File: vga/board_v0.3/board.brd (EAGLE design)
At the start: 55 x 53 mm, 130 parts, among them IC1 XC6S{9,16,25}LX-FT256, IC2 74LVC3G34, IC3 AS4C8M16D1

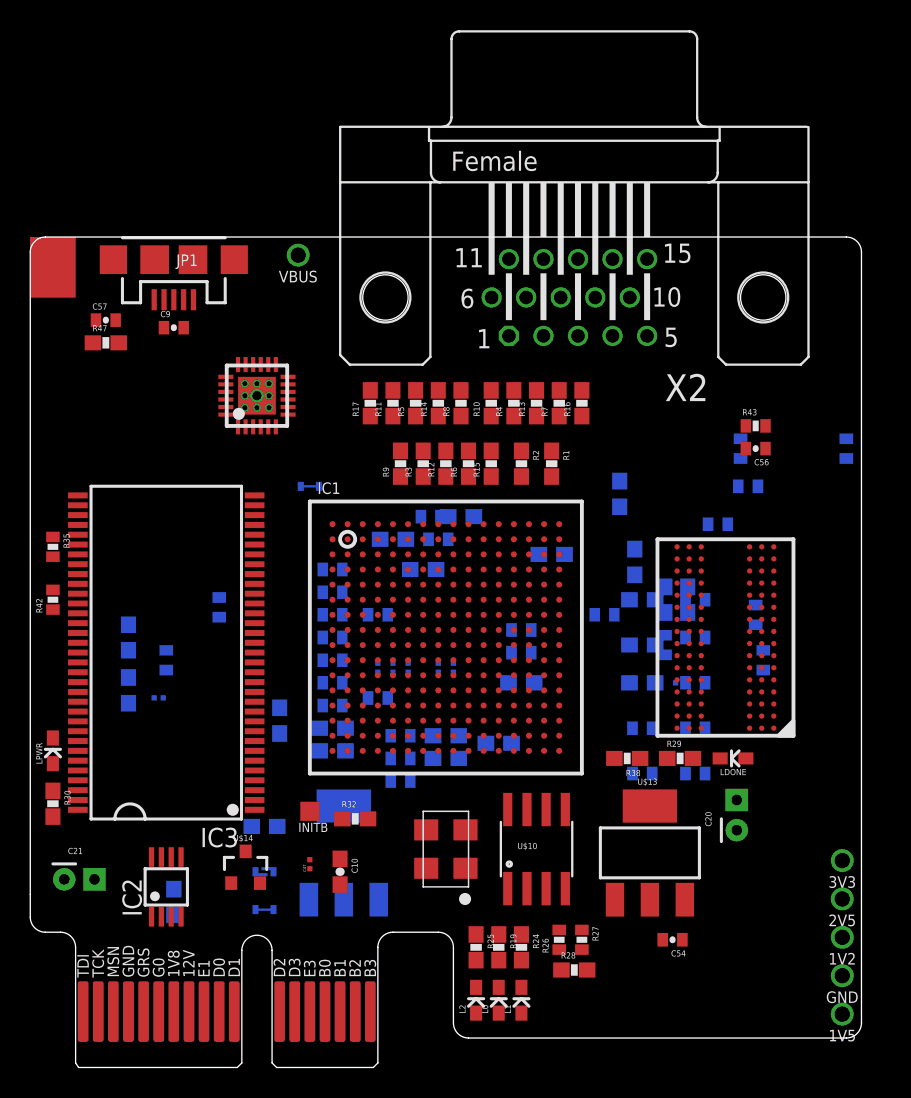
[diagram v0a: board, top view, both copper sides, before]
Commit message: vga board v0.3.  added keepout to a bunch of packages
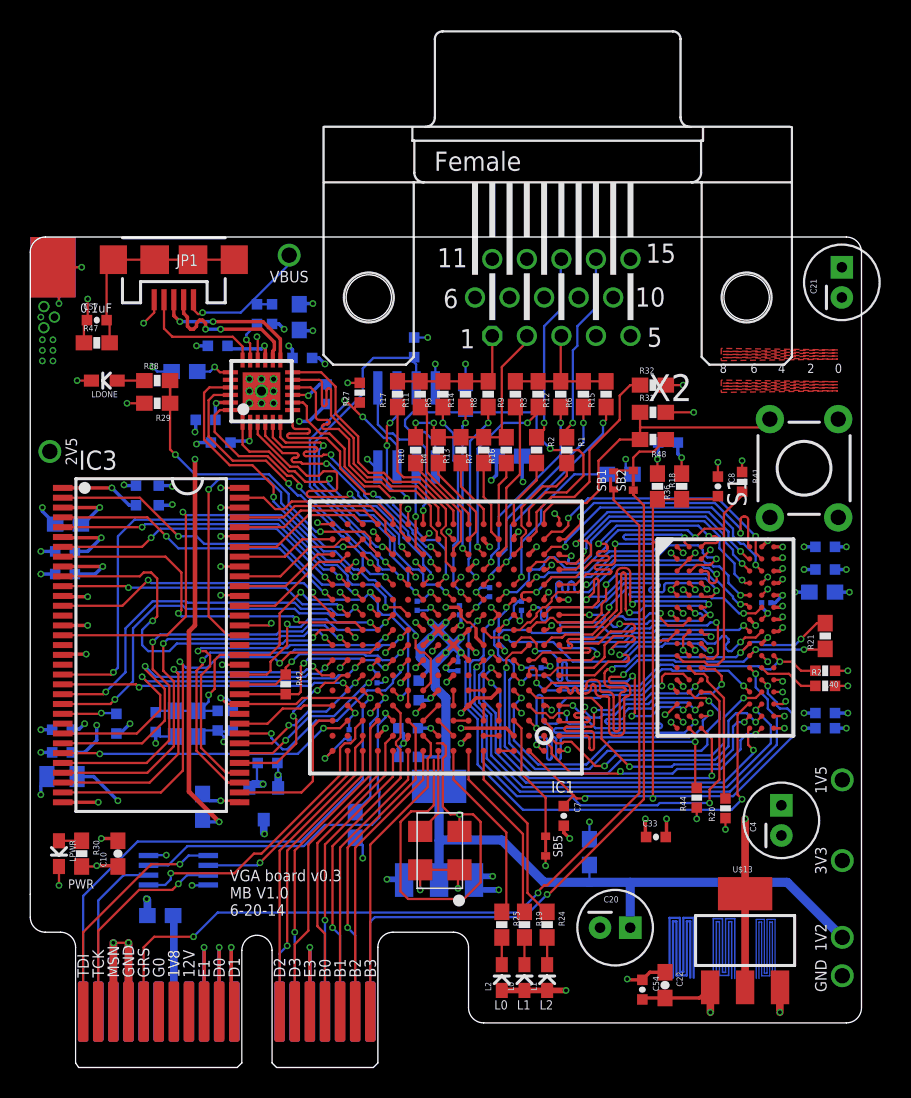
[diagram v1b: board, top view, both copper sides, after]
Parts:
- removed C28, C50: 10uF, kmod-passives:0603-CAP
- removed C29, C31, C32: 1uF, kmod-passives:0402-CAP
- removed CONN6: INITB, kmod-nonparts:TESTPAD-1.27
- added R48: 100, kmod-passives:0603-RES
- added S1: TAC_SWITCHPTH, kmod-mechanical:TACTILE-PTH
- C23: value 10uF -> 22uF; device kmod-passives:0603-CAP -> kmod-passives:0805
- C4: value 10uF -> 100uF; device kmod-passives:0603-CAP -> kmod-passives:CAP-5-2
- C5: value 1uF -> 0.1uF; device kmod-passives:0402-CAP -> kmod-passives:C0201
- R23: device kmod-passives:0603-RES -> kmod-passives:0402-RES
- X2: value (none) -> (none)
- moved C21 64.1 mm to (53.7, 52.0), turned to 90 degrees
- moved CONN2 60.2 mm to (1.30, 40.8), turned to 90 degrees
- moved LDONE 48.5 mm to (4.90, 45.5)
- moved C53 42.4 mm to (11.6, 42.9), turned to 0 degrees
- moved R29 41.8 mm to (8.40, 44.0), turned to 180 degrees
- moved R26 40.4 mm to (25.4, 47.7), flipped to the bottom, turned to 270 degrees
- moved R38 39.9 mm to (8.40, 45.5), turned to 0 degrees
- moved R27 39.1 mm to (21.8, 44.7), turned to 90 degrees
- moved R28 38.7 mm to (28.8, 44.5), flipped to the bottom, turned to 90 degrees
- moved R31 37.6 mm to (41.2, 43.4), flipped to the top
- moved SB2 37.4 mm to (39.9, 38.9), flipped to the top, turned to 90 degrees
- moved C55 35.3 mm to (12.4, 47.8), turned to 0 degrees
- moved C17 35.0 mm to (12.6, 41.4)
- moved R32 34.8 mm to (41.2, 45.2)
- moved SB1 34.7 mm to (38.6, 38.9), flipped to the top, turned to 90 degrees
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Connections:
- net N$12 renamed DDR3_ZQ
- net N$13 renamed DDR3_CS#
- new net N$17: IC1.A4, IC1.A5
- new net N$22: IC1.B5, IC1.B6
- new net N$24: IC1.C5, IC1.D5
- new net N$25: IC1.C6, IC1.D6
- new net N$26: IC1.C7, IC1.C8
- new net N$27: IC1.B8, IC1.C9
- new net N$28: IC1.C10, IC1.D9
- new net N$29: IC1.D8, IC1.E8
- new net N$31: IC1.E6, IC1.E7
- new net N$32: IC1.D11, IC1.E11
- new net N$35: R48.1, SB1.R1, SB1.R2, SB2.R1
- net 1.2V: now also C20.1; no longer C4.1, C5.1
- net 1.5V: now also C4.1, C5.1, IC1.D2, IC1.G4, IC1.J2, IC1.K4, IC1.N2; no longer C20.1, C28.1, C29.1, C50.1, IC1.D15, IC1.G13, IC1.J15, IC1.K13, IC1.N15, IC1.R13
- net 2.5V: now also IC1.D15, IC1.G13, IC1.J15, IC1.K13, IC1.N15, IC1.R13; no longer C21.1, IC1.D2, IC1.G4, IC1.J2, IC1.K4, IC1.N2
- net 3.3V: now also C21.1
- net 50MHZ: now also IC1.A9
- net DDR1_A0: now also IC1.H15; no longer IC1.K5
- net DDR1_A1: now also IC1.H16; no longer IC1.K6
- net DDR1_A10: now also IC1.C15; no longer IC1.G6
- net DDR1_A11: now also IC1.G11; no longer IC1.E3
- net DDR1_A12: now also IC1.D16; no longer IC1.F3
- net DDR1_A2: now also IC1.F16; no longer IC1.D1
- net DDR1_A3: now also IC1.H13; no longer IC1.L4
- net DDR1_A4: now also IC1.C16; no longer IC1.G5
- net DDR1_A5: now also IC1.J11; no longer IC1.H4
- net DDR1_A6: now also IC1.J12; no longer IC1.H3
- net DDR1_A7: now also IC1.F15; no longer IC1.D3
- net DDR1_A8: now also IC1.F13; no longer IC1.B2
- net DDR1_A9: now also IC1.F14; no longer IC1.A2
- net DDR1_BA0: now also IC1.G14; no longer IC1.C3
- net DDR1_BA1: now also IC1.G16; no longer IC1.C2
- net DDR1_CAS#: now also IC1.K14; no longer IC1.H5
- net DDR1_CK: now also IC1.G12; no longer IC1.E2
- net DDR1_CK#: now also IC1.H11; no longer IC1.E1
- net DDR1_CKE: now also IC1.D14; no longer IC1.F4
- net DDR1_DML: now also IC1.K11; no longer IC1.J4
- net DDR1_DMU: now also IC1.K12; no longer IC1.K3
- net DDR1_DQ0: now also IC1.L14; no longer IC1.K2
- net DDR1_DQ1: now also IC1.L16; no longer IC1.K1
- net DDR1_DQ10: now also IC1.R15; no longer IC1.M2
- net DDR1_DQ11: now also IC1.R16; no longer IC1.M1
- net DDR1_DQ12: now also IC1.T14; no longer IC1.P2
- net DDR1_DQ13: now also IC1.T13; no longer IC1.P1
- net DDR1_DQ14: now also IC1.R12; no longer IC1.R2
- net DDR1_DQ15: now also IC1.T12; no longer IC1.R1
- net DDR1_DQ2: now also IC1.M15; no longer IC1.J3
- net DDR1_DQ3: now also IC1.M16; no longer IC1.J1
- net DDR1_DQ4: now also IC1.J14; no longer IC1.F2
- net DDR1_DQ5: now also IC1.J16; no longer IC1.F1
- net DDR1_DQ6: now also IC1.K15; no longer IC1.G3
- net DDR1_DQ7: now also IC1.K16; no longer IC1.G1
- net DDR1_DQ8: now also IC1.P15; no longer IC1.L3
- net DDR1_DQ9: now also IC1.P16; no longer IC1.L1
- net DDR1_DQSL: now also IC1.N14; no longer IC1.H2
- net DDR1_DQSU: now also IC1.R14; no longer IC1.N3
- net DDR1_RAS#: now also IC1.J13; no longer IC1.J6
- net DDR1_WE#: now also IC1.E15; no longer IC1.C1
- net DDR3_A0: now also IC1.K5; no longer IC1.H15
- net DDR3_A1: now also IC1.K6; no longer IC1.H16
- net DDR3_A10: now also IC1.G6; no longer IC1.C15
- net DDR3_A11: now also IC1.E3; no longer IC1.G11
- net DDR3_A12: now also IC1.F3; no longer IC1.D16
- net DDR3_A13: now also IC1.F6; no longer IC1.B15
- net DDR3_A14: now also IC1.F5; no longer IC1.B16
- net DDR3_A2: now also IC1.D1; no longer IC1.F16
- net DDR3_A3: now also IC1.L4; no longer IC1.H13
- net DDR3_A4: now also IC1.G5; no longer IC1.C16
- net DDR3_A5: now also IC1.H4; no longer IC1.J11
- net DDR3_A6: now also IC1.H3; no longer IC1.J12
- net DDR3_A7: now also IC1.D3; no longer IC1.F15
- net DDR3_A8: now also IC1.B2; no longer IC1.F13
- net DDR3_A9: now also IC1.A2; no longer IC1.F14
- net DDR3_BA0: now also IC1.C3; no longer IC1.G14
- net DDR3_BA1: now also IC1.C2; no longer IC1.G16
- net DDR3_BA2: now also IC1.B1; no longer IC1.E16
- net DDR3_CAS#: now also IC1.H5; no longer IC1.K14
- net DDR3_CK: now also IC1.E2; no longer IC1.G12
- net DDR3_CK#: now also IC1.E1; no longer IC1.H11
- net DDR3_CKE: now also IC1.F4; no longer IC1.D14
- net DDR3_DML: now also IC1.J4; no longer IC1.K11
- net DDR3_DMU: now also IC1.K3; no longer IC1.K12
- net DDR3_DQ0: now also IC1.K2; no longer IC1.L14
- net DDR3_DQ1: now also DDR3_0.F2, IC1.K1; no longer DDR3_0.F7, IC1.L16
- net DDR3_DQ10: now also DDR3_0.A3, IC1.M2; no longer DDR3_0.C8, IC1.R15
- net DDR3_DQ11: now also DDR3_0.A2, IC1.M1; no longer DDR3_0.C2, IC1.R16
- net DDR3_DQ12: now also DDR3_0.C8, IC1.P2; no longer DDR3_0.A7, IC1.T14
- net DDR3_DQ13: now also DDR3_0.D7, IC1.P1; no longer DDR3_0.A2, IC1.T13
- net DDR3_DQ14: now also IC1.R2; no longer IC1.R12
- net DDR3_DQ15: now also DDR3_0.A7, IC1.R1; no longer DDR3_0.A3, IC1.T12
- net DDR3_DQ2: now also DDR3_0.F7, IC1.J3; no longer DDR3_0.F2, IC1.M15
- net DDR3_DQ3: now also IC1.J1; no longer IC1.M16
- net DDR3_DQ4: now also IC1.F2; no longer IC1.J14
- net DDR3_DQ5: now also IC1.F1; no longer IC1.J16
- net DDR3_DQ6: now also IC1.G3; no longer IC1.K15
- net DDR3_DQ7: now also IC1.G1; no longer IC1.K16
- net DDR3_DQ8: now also DDR3_0.C2, IC1.L3; no longer DDR3_0.D7, IC1.P15
- net DDR3_DQ9: now also IC1.L1; no longer IC1.P16
- net DDR3_DQSL: now also IC1.H2; no longer IC1.N14
- net DDR3_DQSL#: now also IC1.H1; no longer IC1.N16
- net DDR3_DQSU: now also IC1.N3; no longer IC1.R14
- net DDR3_DQSU#: now also IC1.N1; no longer IC1.T15
- net DDR3_ODT: now also IC1.L5; no longer IC1.H14
- net DDR3_RAS#: now also IC1.J6; no longer IC1.J13
- net DDR3_RESET#: now also IC1.E4; no longer IC1.F12
- net DDR3_WE#: now also IC1.C1; no longer IC1.E15
- net GND: now also S1.3, U$3.A10, U$3.A11, U$3.A14, U$3.A9, U$3.B10, U$3.B11, U$3.B14, U$3.B9; no longer C28.2, C29.2, C31.2, C32.2, C50.2
- net HSYNC: now also IC1.T4; no longer IC1.A10
- net INIT_B: no longer CONN6.P
- net L0: now also IC1.A8
- net L1: now also IC1.A7
- net L2: now also IC1.A6
- net MB_A0: now also IC1.A12; no longer IC1.P7, SB2.L1
- net MB_A1: now also IC1.D12; no longer IC1.P8
- net MB_A2: now also IC1.C11; no longer IC1.R9
- net MB_A3: now also SB2.L1; no longer IC1.P9
- net MB_B0: now also IC1.B12; no longer IC1.T6
- net MB_B1: now also IC1.A11; no longer IC1.T7
- net MB_B2: now also IC1.A10; no longer IC1.T8
- net MB_B3: now also IC1.B10; no longer IC1.T9
- net MB_C2: now also IC1.A14; no longer IC1.R5
- net MB_C3: now also IC1.C13; no longer IC1.R7
- net MB_D2: now also IC1.B14; no longer IC1.T4
- net MB_D3: now also IC1.A13; no longer IC1.T5
- net PROGRAM: now also R48.2, S1.2; no longer SB1.R1, SB1.R2, SB2.R1
- net USB_CLK: now also IC1.E10; no longer IC1.A8
- net USB_DATA0: now also IC1.M10; no longer IC1.B5
- net USB_DATA1: now also IC1.N9; no longer IC1.A5
- net USB_DATA2: now also IC1.L10; no longer IC1.D5
- net USB_DATA3: now also IC1.P9; no longer IC1.C5
- net USB_DATA4: now also IC1.M9; no longer IC1.B6
- net USB_DATA5: now also IC1.R9; no longer IC1.A6
- net USB_DATA6: now also IC1.T9; no longer IC1.C7
- net USB_DATA7: now also IC1.N8; no longer IC1.A7
- net USB_DIR: now also IC1.L8; no longer IC1.C6
- net USB_NXT: now also IC1.P11; no longer IC1.D6
- net USB_RESET: now also IC1.M12; no longer IC1.A4
- net USB_STP: now also IC1.M11; no longer IC1.B8
- net VB0: now also IC1.N5; no longer IC1.A14
- net VB1: now also IC1.N6; no longer IC1.D11
- net VB2: now also IC1.P5; no longer IC1.D12
- net VB3: now also IC1.M6; no longer IC1.C9
- net VB4: now also IC1.P6; no longer IC1.A9
- net VG0: now also IC1.T5; no longer IC1.C13
- net VG1: now also IC1.T6; no longer IC1.A13
- net VG2: now also IC1.P8; no longer IC1.F10
- net VG3: now also IC1.R5; no longer IC1.E11
- net VG4: now also IC1.R7; no longer IC1.B14
- net VR0: now also IC1.T8; no longer IC1.A11
- net VR1: now also IC1.P7; no longer IC1.F9
- net VR2: now also IC1.T7; no longer IC1.D9
- net VR3: now also IC1.M7; no longer IC1.B12
- net VR4: now also IC1.L7; no longer IC1.A12
- net VREF_DDR1: now also IC1.E12, IC1.L13; no longer C32.1, IC1.A3, IC1.M3
- net VREF_DDR3: now also IC1.A3, IC1.M3; no longer C31.1, IC1.E12, IC1.L13
- net VSYNC: now also IC1.P4; no longer IC1.C10
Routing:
- net GND: track 0.00 -> 220.0 mm, vias 0 -> 121
- net 3.3V: track 0.00 -> 90.8 mm, vias 0 -> 42
- net 1.2V: track 0.00 -> 72.0 mm, vias 0 -> 7
- net VREF_DDR3: track 0.00 -> 62.9 mm, vias 0 -> 5
- net !GRST: track 0.00 -> 62.7 mm, vias 0 -> 2
- net MB_A3: track 0.00 -> 48.1 mm, vias 0 -> 1
- net 2.5V: track 0.00 -> 41.2 mm, vias 0 -> 21
- net 1.5V: track 0.00 -> 39.4 mm, vias 0 -> 30
- net DDR3_A0: track 0.00 -> 36.6 mm, vias 0 -> 3
- net DDR3_A1: track 0.00 -> 36.6 mm, vias 0 -> 2
- net TDO: track 0.00 -> 35.7 mm, vias 0 -> 1
- net DDR1_DML: track 0.00 -> 35.4 mm, vias 0 -> 2
- net DDR3_A10: track 0.00 -> 34.3 mm, vias 0 -> 2
- net DDR3_ODT: track 0.00 -> 33.5 mm, vias 0 -> 2
- net DDR3_A4: track 0.00 -> 31.9 mm, vias 0 -> 2
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- added copper zone on layer 15, net 1.5V
- added copper zone on layer 15, net 2.5V
- added copper zone on layer 15, net 3.3V
- added copper zone on layer 1, net N$23
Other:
- board size 55 x 53 mm -> 55 x 52 mm
- board text added: "0"
- board text added: "0.1uF"
- board text added: "2"
- board text added: "3/4"
- board text added: "4"
- board text added: "4/4"
- board text added: "6"
- board text added: "6/3"
- board text added: "8"
- board text added: "L0"
- board text added: "L1"
- board text added: "L2"
- board text added: "PWR"
- board text added: "VGA board v0.3 MB V1.0 6-20-14"

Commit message: Initial coven boards: A13 v0.1 card and test socket
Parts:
- R12, R13, R14: value 3.9k -> 4.02k
- R15, R16, R17: value 8.2k -> 8.06k
- R26: value 10k DNP -> 10k
- R27: value 10k DNP -> DNP(10k)
- R28: value 2.4k -> 10k
- R3, R4, R5: value 510 -> 499
- U$14: value MCP1700-2502 -> MCP1700T-2502
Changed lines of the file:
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@@
 <?xml version="1.0" encoding="utf-8"?>
 <!DOCTYPE eagle SYSTEM "eagle.dtd">
-<eagle version="6.4">
+<eagle version="6.5.0">
 <drawing>
 <settings>
@@
 <setting verticaltext="up"/>
 </settings>
-<grid distance="0.1" unitdist="mm" unit="mm" style="lines" multiple="1" display="yes" altdistance="0.3" altunitdist="mm" altunit="mm"/>
+<grid distance="0.5" unitdist="mm" unit="mm" style="lines" multiple="1" display="yes" altdistance="0.01" altunitdist="mm" altunit="mm"/>
 <layers>
 <layer number="1" name="Top" color="4" fill="1" visible="yes" active="yes"/>
-<layer number="2" name="Route2" color="5" fill="5" visible="yes" active="yes"/>
+<layer number="2" name="Route2" color="20" fill="5" visible="yes" active="yes"/>
 <layer number="3" name="Route3" color="4" fill="3" visible="no" active="no"/>
 <layer number="4" name="Route4" color="1" fill="4" visible="no" active="no"/>
@@
 <layer number="13" name="Route13" color="4" fill="5" visible="no" active="no"/>
 <layer number="14" name="Route14" color="1" fill="6" visible="no" active="no"/>
-<layer number="15" name="Route15" color="3" fill="4" visible="yes" active="yes"/>
+<layer number="15" name="Route15" color="5" fill="4" visible="yes" active="yes"/>
 <layer number="16" name="Bottom" color="1" fill="1" visible="yes" active="yes"/>
 <layer number="17" name="Pads" color="2" fill="1" visible="yes" active="yes"/>
@@
 <attribute name="OC_FARNELL" value="unknown" x="34.9" y="57" size="1.778" layer="27" rot="R180" display="off"/>
 </element>
-<element name="R3" library="kmod-passives" package="0603-RES" value="510" x="33.6" y="44.6" rot="R90"/>
-<element name="R4" library="kmod-passives" package="0603-RES" value="510" x="27" y="40.9" rot="R90"/>
-<element name="R5" library="kmod-passives" package="0603-RES" value="510" x="27.3" y="44.6" rot="R90"/>
+<element name="R3" library="kmod-passives" package="0603-RES" value="499" x="33.6" y="44.6" rot="R90"/>
+<element name="R4" library="kmod-passives" package="0603-RES" value="499" x="27" y="40.9" rot="R90"/>
+<element name="R5" library="kmod-passives" package="0603-RES" value="499" x="27.3" y="44.6" rot="R90"/>
 <element name="R6" library="kmod-passives" package="0603-RES" value="1k" x="36.6" y="44.6" rot="R90"/>
 <element name="R7" library="kmod-passives" package="0603-RES" value="1k" x="30" y="40.9" rot="R90"/>
@@
 <element name="R10" library="kmod-passives" package="0603-RES" value="2k" x="25.5" y="40.9" rot="R90"/>
 <element name="R11" library="kmod-passives" package="0603-RES" value="2k" x="25.8" y="44.6" rot="R90"/>
-<element name="R12" library="kmod-passives" package="0603-RES" value="3.9k" x="35.1" y="44.6" rot="R90"/>
-<element name="R13" library="kmod-passives" package="0603-RES" value="3.9k" x="28.5" y="40.9" rot="R90"/>
-<element name="R14" library="kmod-passives" package="0603-RES" value="3.9k" x="28.8" y="44.6" rot="R90"/>
-<element name="R15" library="kmod-passives" package="0603-RES" value="8.2k" x="38.1" y="44.6" rot="R90"/>
-<element name="R16" library="kmod-passives" package="0603-RES" value="8.2k" x="31.5" y="40.9" rot="R90"/>
-<element name="R17" library="kmod-passives" package="0603-RES" value="8.2k" x="24.3" y="44.6" rot="R90"/>
+<element name="R12" library="kmod-passives" package="0603-RES" value="4.02k" x="35.1" y="44.6" rot="R90"/>
+<element name="R13" library="kmod-passives" package="0603-RES" value="4.02k" x="28.5" y="40.9" rot="R90"/>
+<element name="R14" library="kmod-passives" package="0603-RES" value="4.02k" x="28.8" y="44.6" rot="R90"/>
+<element name="R15" library="kmod-passives" package="0603-RES" value="8.06k" x="38.1" y="44.6" rot="R90"/>
+<element name="R16" library="kmod-passives" package="0603-RES" value="8.06k" x="31.5" y="40.9" rot="R90"/>
+<element name="R17" library="kmod-passives" package="0603-RES" value="8.06k" x="24.3" y="44.6" rot="R90"/>
 <element name="C9" library="kmod-passives" package="0402-CAP" value="1uF" x="18" y="47" rot="MR0"/>
 <element name="C10" library="kmod-passives" package="0603-CAP" value="10uF" x="5.8" y="14.2" rot="R90"/>
@@
 <element name="R23" library="kmod-passives" package="0402-RES" value="240 1%" x="52.6" y="25.3"/>
 <element name="U$10" library="kmod-ics" package="SO08" value="M25P80/W25Q80" x="24.9" y="42.4" rot="MR0"/>
-<element name="R26" library="kmod-passives" package="0402-RES" value="10k DNP" x="25.4" y="47.7" rot="MR270"/>
-<element name="R27" library="kmod-passives" package="0402-RES" value="10k DNP" x="21.8" y="44.7" rot="R90"/>
-<element name="R28" library="kmod-passives" package="0603-RES" value="2.4k" x="28.8" y="44.5" rot="MR90"/>
+<element name="R26" library="kmod-passives" package="0402-RES" value="10k" x="25.4" y="47.7" rot="MR270"/>
+<element name="R27" library="kmod-passives" package="0402-RES" value="DNP(10k)" x="21.8" y="44.7" rot="R90"/>
+<element name="R28" library="kmod-passives" package="0603-RES" value="10k" x="28.8" y="44.5" rot="MR90"/>
 <element name="R29" library="kmod-passives" package="0603-RES" value="220" x="8.4" y="44" rot="R180"/>
 <element name="LDONE" library="kmod-passives" package="0603_LED" value="GRN" x="4.9" y="45.5" rot="R90"/>
@@
 <element name="R44" library="kmod-passives" package="0402-RES" value="4.7k" x="44.1" y="17.9" rot="R90"/>
 <element name="R46" library="kmod-passives" package="0603-RES" value="0.01R" x="8.6" y="10.1" rot="MR0"/>
-<element name="U$14" library="kmod-ics" package="SOT23-3" value="MCP1700-2502" x="15.45" y="17.55" rot="MR180"/>
+<element name="U$14" library="kmod-ics" package="SOT23-3" value="MCP1700T-2502" x="15.45" y="17.55" rot="MR180"/>
 <element name="C22" library="kmod-passives" package="0603-CAP" value="10uF" x="42" y="5.5" rot="R270"/>
 <element name="C23" library="kmod-passives" package="0805" value="22uF" x="2.1" y="19.3" rot="MR180"/>
